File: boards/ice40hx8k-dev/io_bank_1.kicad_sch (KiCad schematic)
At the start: 22 parts, among them U1 ICE40HX8K-CT256

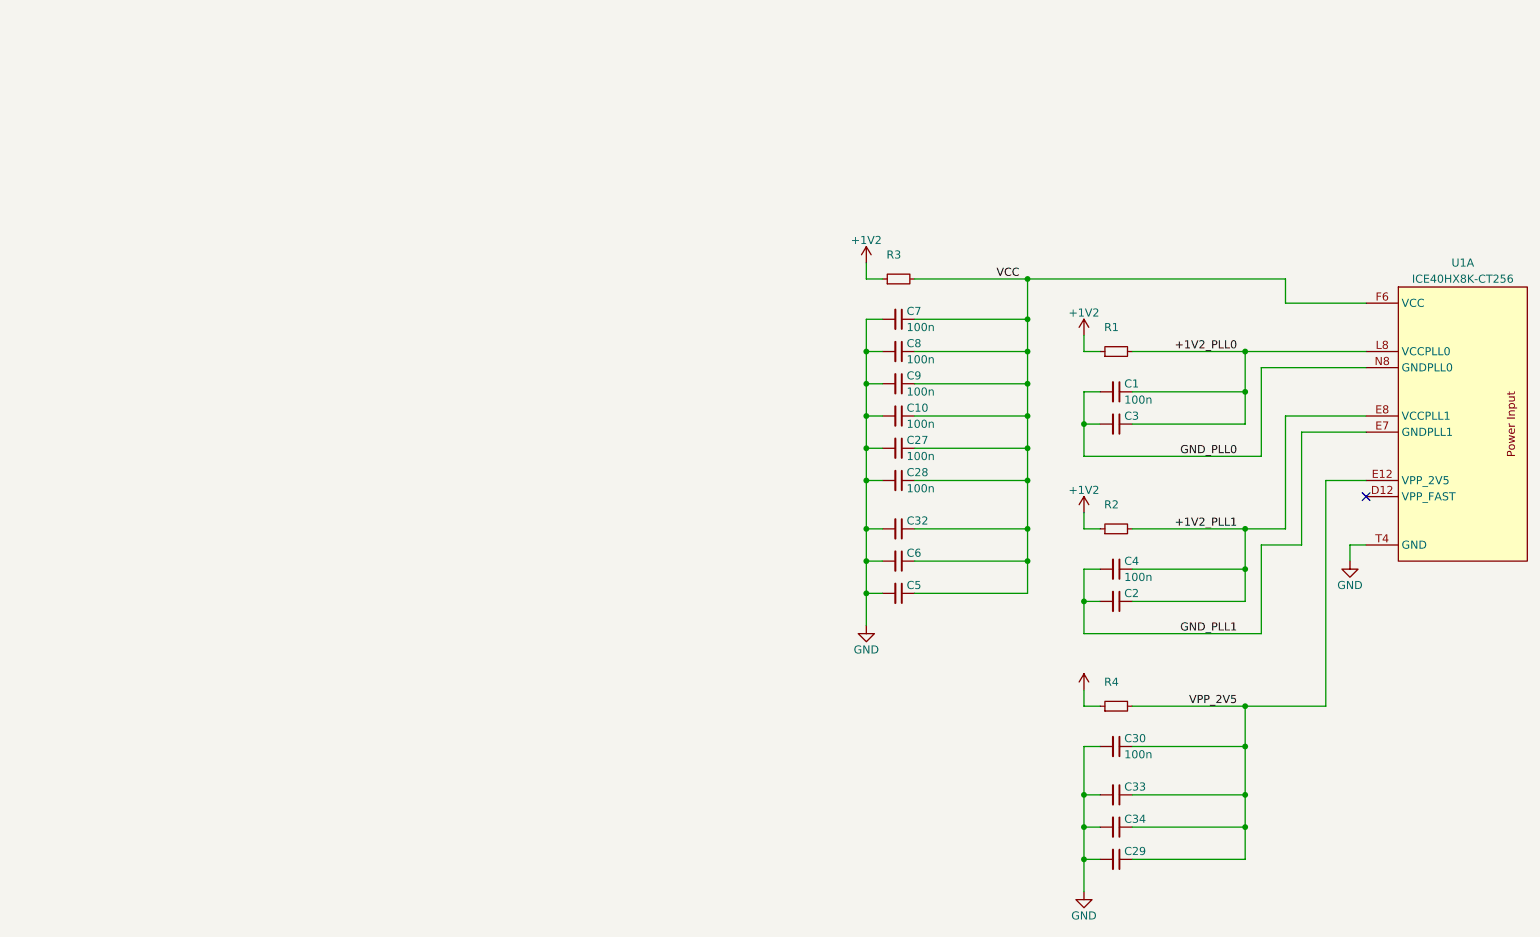
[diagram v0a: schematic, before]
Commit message: Split up schematic and label all nets.
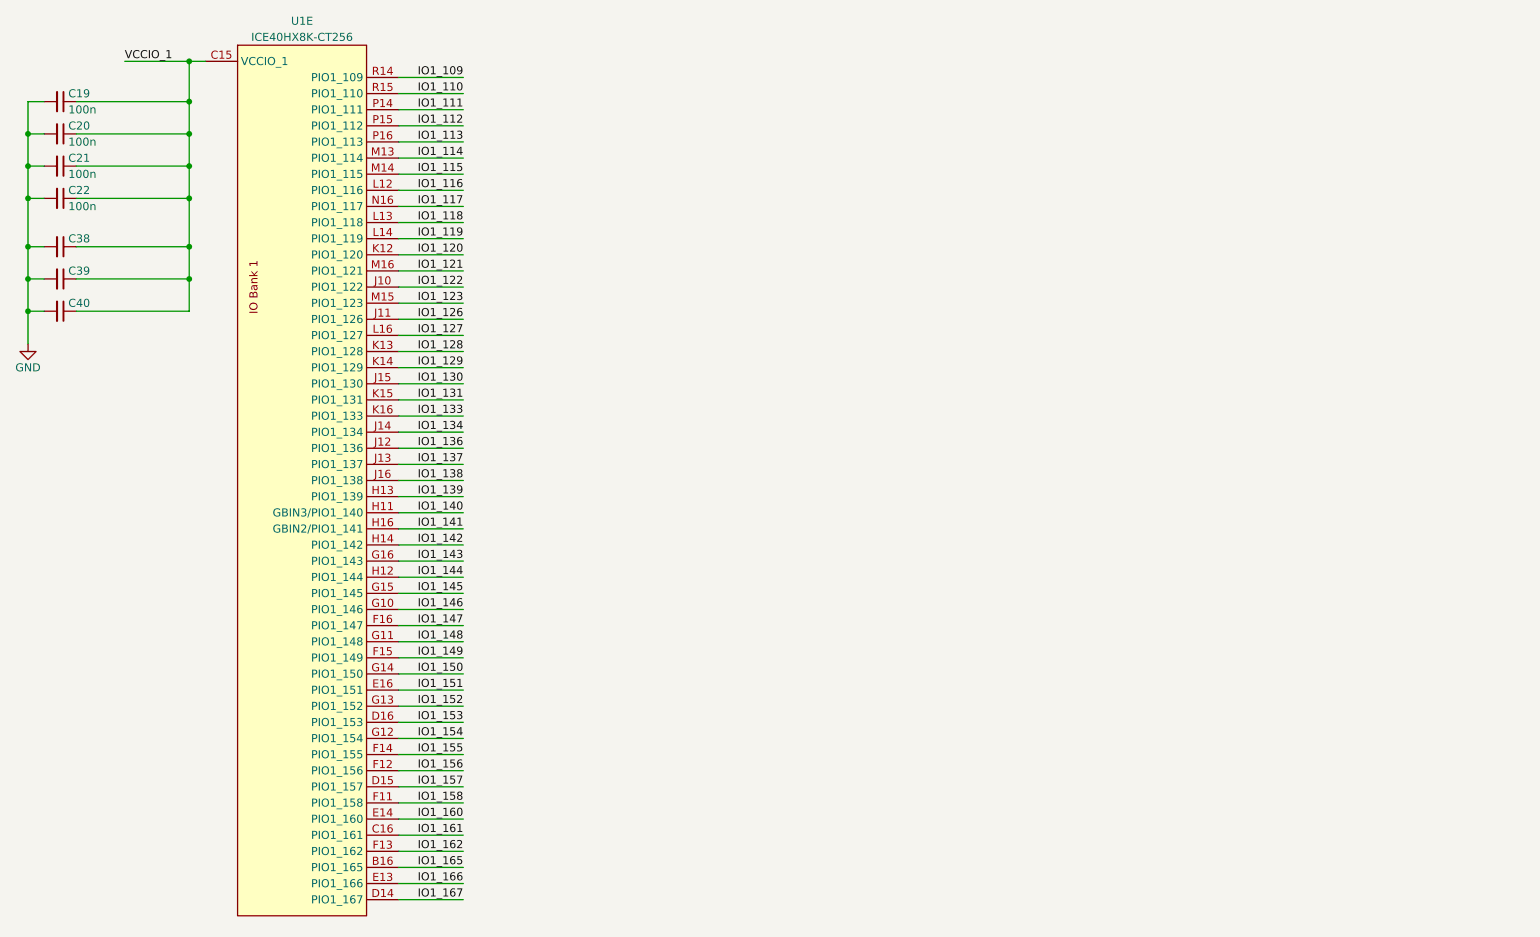
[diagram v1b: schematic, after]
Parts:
- removed C1, C10, C27, C28, C30, C4, C7, C8, C9: 100n, 0Local:C_SMD_0402_Pad0.5mm, symbol Device:C_Small
- removed C2, C29, C3, C32, C33, C34, C5, C6: (no value), 0Local:C_SMD_0402_Pad0.5mm, symbol Device:C_Small
- removed R1, R3: (no value), 0Local:R_SMD_0402_Pad0.5mm, symbol Device:R_Small
- removed R2, R4: (no value), symbol Device:R_Small
- removed U1: ICE40HX8K-CT256, 0Local:Lattice_caBGA-256_14x14mm_Layout16x16_P0.8mm_Ball0.4mm_Pad0.5mm_SMD, symbol 0Local:ICE40HX8K-CT256
- added C19, C20, C21, C22: 100n, 0Local:C_SMD_0402_Pad0.5mm, symbol Device:C_Small
- added C38, C39, C40: (no value), 0Local:C_SMD_0402_Pad0.5mm, symbol Device:C_Small
- added U1: ICE40HX8K-CT256, 0Local:Lattice_caBGA-256_14x14mm_Layout16x16_P0.8mm_Ball0.4mm_Pad0.5mm_SMD, symbol 0Local:ICE40HX8K-CT256
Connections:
- net GND: now also C19.2, C20.2, C21.2, C22.2, C38.2, C39.2, C40.2
- new net IO1_109: U1.R14 (PIO1_109)
- new net IO1_110: U1.R15 (PIO1_110)
- new net IO1_111: U1.P14 (PIO1_111)
- new net IO1_112: U1.P15 (PIO1_112)
- new net IO1_113: U1.P16 (PIO1_113)
- new net IO1_114: U1.M13 (PIO1_114)
- new net IO1_115: U1.M14 (PIO1_115)
- new net IO1_116: U1.L12 (PIO1_116)
- new net IO1_117: U1.N16 (PIO1_117)
- new net IO1_118: U1.L13 (PIO1_118)
- new net IO1_119: U1.L14 (PIO1_119)
- new net IO1_120: U1.K12 (PIO1_120)
- new net IO1_121: U1.M16 (PIO1_121)
- new net IO1_122: U1.J10 (PIO1_122)
- new net IO1_123: U1.M15 (PIO1_123)
- new net IO1_126: U1.J11 (PIO1_126)
- new net IO1_127: U1.L16 (PIO1_127)
- new net IO1_128: U1.K13 (PIO1_128)
- new net IO1_129: U1.K14 (PIO1_129)
- new net IO1_130: U1.J15 (PIO1_130)
- new net IO1_131: U1.K15 (PIO1_131)
- new net IO1_133: U1.K16 (PIO1_133)
- new net IO1_134: U1.J14 (PIO1_134)
- new net IO1_136: U1.J12 (PIO1_136)
- new net IO1_137: U1.J13 (PIO1_137)
- new net IO1_138: U1.J16 (PIO1_138)
- new net IO1_139: U1.H13 (PIO1_139)
- new net IO1_140: U1.H11 (GBIN3/PIO1_140)
- new net IO1_141: U1.H16 (GBIN2/PIO1_141)
- new net IO1_142: U1.H14 (PIO1_142)
- new net IO1_143: U1.G16 (PIO1_143)
- new net IO1_144: U1.H12 (PIO1_144)
- new net IO1_145: U1.G15 (PIO1_145)
- new net IO1_146: U1.G10 (PIO1_146)
- new net IO1_147: U1.F16 (PIO1_147)
- new net IO1_148: U1.G11 (PIO1_148)
- new net IO1_149: U1.F15 (PIO1_149)
- new net IO1_150: U1.G14 (PIO1_150)
- new net IO1_151: U1.E16 (PIO1_151)
- new net IO1_152: U1.G13 (PIO1_152)
- new net IO1_153: U1.D16 (PIO1_153)
- new net IO1_154: U1.G12 (PIO1_154)
- new net IO1_155: U1.F14 (PIO1_155)
- new net IO1_156: U1.F12 (PIO1_156)
- new net IO1_157: U1.D15 (PIO1_157)
- new net IO1_158: U1.F11 (PIO1_158)
- new net IO1_160: U1.E14 (PIO1_160)
- new net IO1_161: U1.C16 (PIO1_161)
- new net IO1_162: U1.F13 (PIO1_162)
- new net IO1_165: U1.B16 (PIO1_165)
- new net IO1_166: U1.E13 (PIO1_166)
- new net IO1_167: U1.D14 (PIO1_167)
- new net VCCIO_1: C19.1, C20.1, C21.1, C22.1, C38.1, C39.1, C40.1, U1.C15 (VCCIO_1), U1.H10 (VCCIO_1), U1.H15 (VCCIO_1), U1.N15 (VCCIO_1)
- no-connect marks 1 -> 0

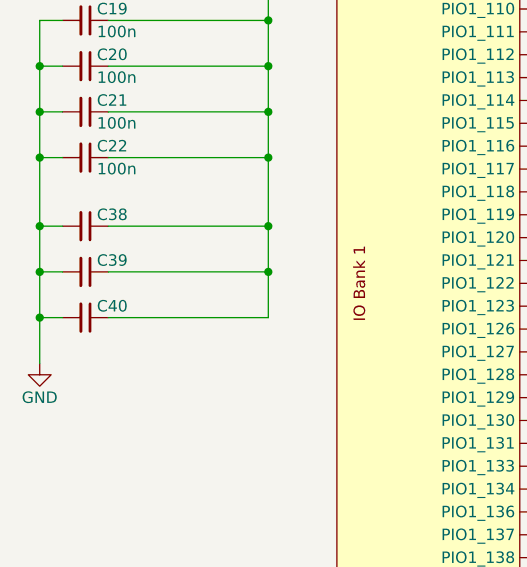
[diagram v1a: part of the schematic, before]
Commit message: Switch to 6 layers, add power fills under BGA.
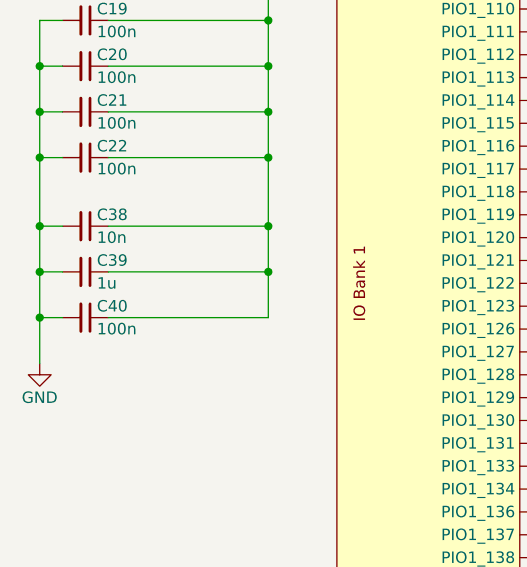
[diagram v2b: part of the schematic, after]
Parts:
- C38: value (none) -> 10n
- C39: value (none) -> 1u
- C40: value (none) -> 100n
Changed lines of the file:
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@@
       (effects (font (size 1.27 1.27)) (justify left))
     )
-    (property "Value" "" (id 1) (at 24.13 58.42 90)
+    (property "Value" "10n" (id 1) (at 24.13 58.42 90)
       (effects (font (size 1.27 1.27)) (justify left))
     )
@@
       (effects (font (size 1.27 1.27)) (justify left))
     )
-    (property "Value" "" (id 1) (at 24.13 63.5 90)
+    (property "Value" "1u" (id 1) (at 24.13 63.5 90)
       (effects (font (size 1.27 1.27)) (justify left))
     )
@@
       (effects (font (size 1.27 1.27)) (justify left))
     )
-    (property "Value" "" (id 1) (at 24.13 68.58 90)
-      (effects (font (size 1.27 1.27)) (justify left))
-    )
+    (property "Value" "100n" (id 1) (at 24.13 68.58 90)
+      (effects (font (size 1.27 1.27)) (justify left))
+    )

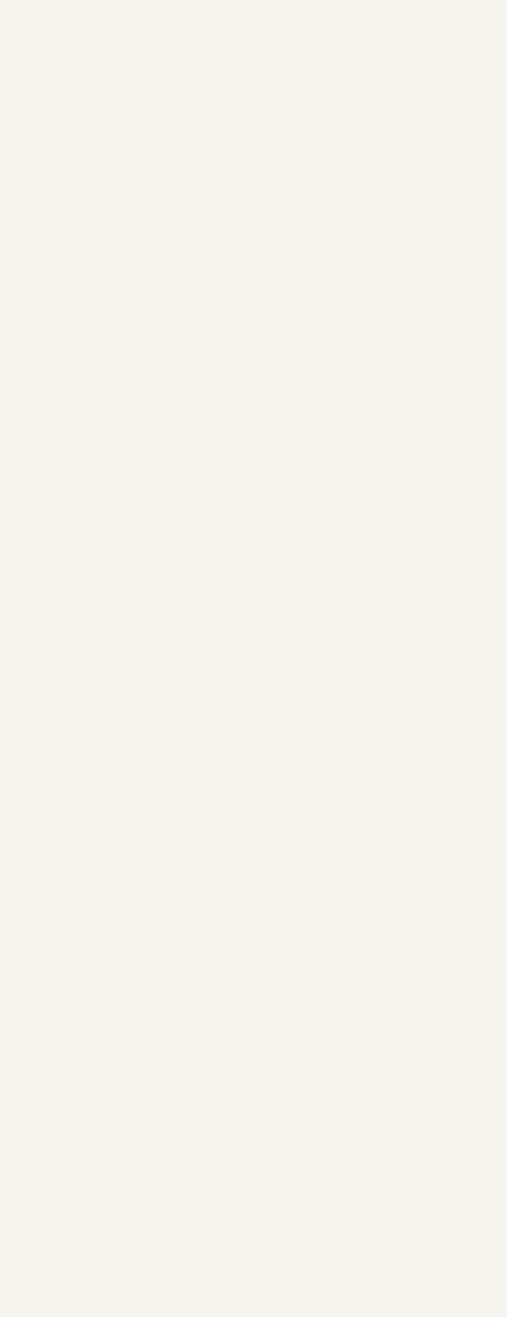
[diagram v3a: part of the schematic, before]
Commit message: Add Hirose connectors and standoffs.
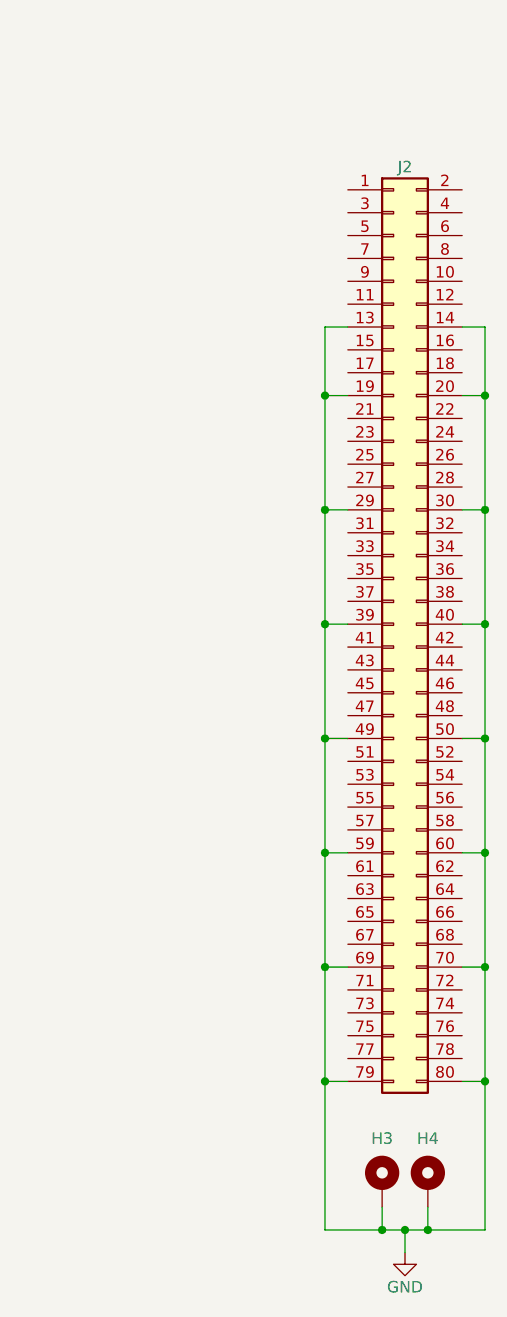
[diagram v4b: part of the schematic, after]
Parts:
- added H3, H4: 9774020633, Mounting_Wuerth:Mounting_Wuerth_WA-SMSI-M1.6_H2mm_9774020633, symbol Mechanical:MountingHole_Pad
- added J2: DF40HC(4.0)-80DS, 0Local:Hirose_DF40C-80DS, symbol Connector_Generic:Conn_02x40_Odd_Even
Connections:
- net GND: now also H3.1, H4.1, J2.13 (Pin_13), J2.14 (Pin_14), J2.19 (Pin_19), J2.20 (Pin_20), J2.29 (Pin_29), J2.30 (Pin_30), J2.39 (Pin_39), J2.40 (Pin_40), J2.49 (Pin_49), J2.50 (Pin_50), J2.59 (Pin_59), J2.60 (Pin_60), J2.69 (Pin_69), J2.70 (Pin_70), J2.79 (Pin_79), J2.80 (Pin_80)

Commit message: Switch to 4mm Hirose connectors and different mounting holes.
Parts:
- H3, H4: footprint Mounting_Wuerth:Mounting_Wuerth_WA-SMSI-M1.6_H2mm_9774020633 -> 0Local:MountingHole_2.2mm_M2_Pad6mm
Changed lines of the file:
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@@
       (effects (font (size 1.27 1.27)) hide)
     )
-    (property "Footprint" "Mounting_Wuerth:Mounting_Wuerth_WA-SMSI-M1.6_H2mm_9774020633" (id 2) (at 238.76 149.86 0)
+    (property "Footprint" "0Local:MountingHole_2.2mm_M2_Pad6mm" (id 2) (at 238.76 149.86 0)
       (effects (font (size 1.27 1.27)) hide)
     )
@@
       (effects (font (size 1.27 1.27)) hide)
     )
-    (property "Footprint" "Mounting_Wuerth:Mounting_Wuerth_WA-SMSI-M1.6_H2mm_9774020633" (id 2) (at 243.84 149.86 0)
+    (property "Footprint" "0Local:MountingHole_2.2mm_M2_Pad6mm" (id 2) (at 243.84 149.86 0)
       (effects (font (size 1.27 1.27)) hide)
     )
